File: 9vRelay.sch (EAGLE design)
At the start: 6 parts, among them K1 OJE-SS-109LMH, T1 2N3904

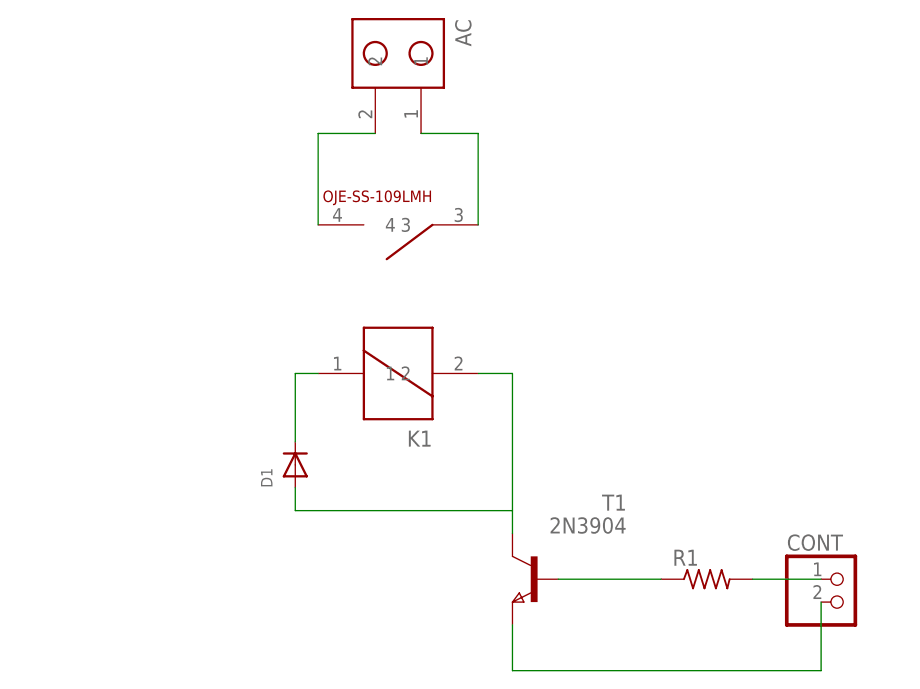
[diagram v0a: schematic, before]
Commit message: Re orientation and fixes
Re orientation and fixed the missing input voltage for powering the relay coil
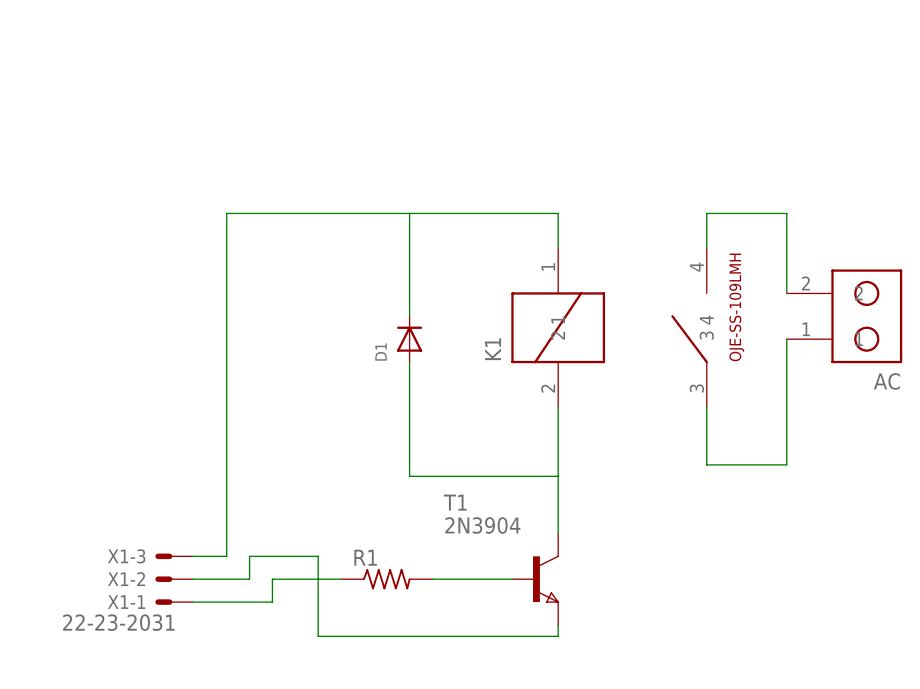
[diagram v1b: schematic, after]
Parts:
- removed CONT: (no value), pinhead:PINHD-1X2
- added X1: 22-23-2031, con-molex:22-23-2031
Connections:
- removed net N$4 (its old number): D1.C, K1.1
- removed net N$6: CONT.2, T1.E
- new net N$2: D1.C, K1.1, X1-3.S
- new net N$3: R1.1, X1-1.S
- net N$7: now also T1.E, X1-2.S; no longer CONT.1, R1.2
- net N$8: now also R1.2; no longer R1.1
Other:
- moved on the sheet: AC, D1, K1, R1
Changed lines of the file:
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@@
 <?xml version="1.0" encoding="utf-8"?>
 <!DOCTYPE eagle SYSTEM "eagle.dtd">
-<eagle version="7.3.0">
+<eagle version="7.4.0">
 <drawing>
 <settings>
@@
 <part name="K1" library="userdefined" deviceset="OJE-SS-109LMH" device=""/>
 <part name="T1" library="zetex" deviceset="FMMT451" device="" value="2N3904"/>
-<part name="CONT" library="pinhead" deviceset="PINHD-1X2" device=""/>
 <part name="AC" library="userdefined" deviceset="TBLOCK1X2" device=""/>
 <part name="R1" library="resistor" deviceset="R-US_" device="R0603"/>
 <part name="D1" library="adafruit" deviceset="DIODE" device="SMA"/>
+<part name="X1" library="con-molex" deviceset="22-23-2031" device=""/>
 </parts>
 <sheets>
@@
 </plain>
 <instances>
-<instance part="K1" gate="G$1" x="38.1" y="43.18" rot="R90"/>
-<instance part="T1" gate="G$1" x="53.34" y="10.16" rot="MR0"/>
-<instance part="CONT" gate="G$1" x="87.63" y="7.62"/>
-<instance part="AC" gate="G$1" x="38.1" y="68.58" rot="R270"/>
-<instance part="R1" gate="G$1" x="72.39" y="10.16"/>
-<instance part="D1" gate="G$1" x="26.67" y="22.86" rot="R90"/>
+<instance part="K1" gate="G$1" x="66.04" y="38.1"/>
+<instance part="T1" gate="G$1" x="53.34" y="10.16"/>
+<instance part="AC" gate="G$1" x="90.17" y="39.37" rot="R180"/>
+<instance part="R1" gate="G$1" x="36.83" y="10.16"/>
+<instance part="D1" gate="G$1" x="39.37" y="36.83" rot="R90"/>
+<instance part="X1" gate="-1" x="12.7" y="7.62" rot="R180"/>
+<instance part="X1" gate="-2" x="12.7" y="10.16" rot="R180"/>
+<instance part="X1" gate="-3" x="12.7" y="12.7" rot="R180"/>
 </instances>
 <busses>
 </busses>
 <nets>
+<net name="N$7" class="0">
+<segment>
+<pinref part="T1" gate="G$1" pin="E"/>
+<wire x1="29.21" y1="3.81" x2="55.88" y2="3.81" width="0.1524" layer="91"/>
+<wire x1="55.88" y1="3.81" x2="55.88" y2="5.08" width="0.1524" layer="91"/>
+<wire x1="29.21" y1="3.81" x2="29.21" y2="12.7" width="0.1524" layer="91"/>
+<wire x1="29.21" y1="12.7" x2="21.59" y2="12.7" width="0.1524" layer="91"/>
+<wire x1="21.59" y1="12.7" x2="21.59" y2="10.16" width="0.1524" layer="91"/>
+<pinref part="X1" gate="-2" pin="S"/>
+<wire x1="21.59" y1="10.16" x2="15.24" y2="10.16" width="0.1524" layer="91"/>
+</segment>
+</net>
+<net name="N$8" class="0">
+<segment>
+<pinref part="R1" gate="G$1" pin="2"/>
+<pinref part="T1" gate="G$1" pin="B"/>
+<wire x1="41.91" y1="10.16" x2="50.8" y2="10.16" width="0.1524" layer="91"/>
+</segment>
+</net>
 <net name="N$1" class="0">
 <segment>
+<pinref part="K1" gate="G$1" pin="2"/>
+<pinref part="T1" gate="G$1" pin="C"/>
+<wire x1="55.88" y1="29.21" x2="55.88" y2="21.59" width="0.1524" layer="91"/>
+<pinref part="D1" gate="G$1" pin="A"/>
+<wire x1="55.88" y1="21.59" x2="55.88" y2="15.24" width="0.1524" layer="91"/>
+<wire x1="39.37" y1="34.29" x2="39.37" y2="21.59" width="0.1524" layer="91"/>
+<wire x1="39.37" y1="21.59" x2="55.88" y2="21.59" width="0.1524" layer="91"/>
+</segment>
+</net>
+<net name="N$2" class="0">
+<segment>
+<pinref part="K1" gate="G$1" pin="1"/>
+<wire x1="55.88" y1="46.99" x2="55.88" y2="50.8" width="0.1524" layer="91"/>
+<pinref part="D1" gate="G$1" pin="C"/>
+<wire x1="55.88" y1="50.8" x2="39.37" y2="50.8" width="0.1524" layer="91"/>
+<wire x1="39.37" y1="50.8" x2="39.37" y2="39.37" width="0.1524" layer="91"/>
+<pinref part="X1" gate="-3" pin="S"/>
+<wire x1="15.24" y1="12.7" x2="19.05" y2="12.7" width="0.1524" layer="91"/>
+<wire x1="19.05" y1="12.7" x2="19.05" y2="50.8" width="0.1524" layer="91"/>
+<wire x1="19.05" y1="50.8" x2="39.37" y2="50.8" width="0.1524" layer="91"/>
+</segment>
+</net>
+<net name="N$4" class="0">
+<segment>
+<pinref part="K1" gate="G$1" pin="4"/>
+<wire x1="72.39" y1="46.99" x2="72.39" y2="50.8" width="0.1524" layer="91"/>
 <pinref part="AC" gate="G$1" pin="2"/>
-<pinref part="K1" gate="G$1" pin="4"/>
-<wire x1="35.56" y1="59.69" x2="29.21" y2="59.69" width="0.1524" layer="91"/>
-<wire x1="29.21" y1="59.69" x2="29.21" y2="49.53" width="0.1524" layer="91"/>
-</segment>
-</net>
-<net name="N$2" class="0">
-<segment>
+<wire x1="72.39" y1="50.8" x2="81.28" y2="50.8" width="0.1524" layer="91"/>
+<wire x1="81.28" y1="50.8" x2="81.28" y2="41.91" width="0.1524" layer="91"/>
+</segment>
+</net>
+<net name="N$11" class="0">
+<segment>
+<wire x1="81.28" y1="22.86" x2="72.39" y2="22.86" width="0.1524" layer="91"/>
+<pinref part="AC" gate="G$1" pin="1"/>
+<wire x1="81.28" y1="36.83" x2="81.28" y2="22.86" width="0.1524" layer="91"/>
 <pinref part="K1" gate="G$1" pin="3"/>
-<wire x1="46.99" y1="49.53" x2="46.99" y2="59.69" width="0.1524" layer="91"/>
-<pinref part="AC" gate="G$1" pin="1"/>
-<wire x1="46.99" y1="59.69" x2="40.64" y2="59.69" width="0.1524" layer="91"/>
+<wire x1="72.39" y1="29.21" x2="72.39" y2="22.86" width="0.1524" layer="91"/>
 </segment>
 </net>
 <net name="N$3" class="0">
 <segment>
-<pinref part="T1" gate="G$1" pin="C"/>
-<wire x1="50.8" y1="15.24" x2="50.8" y2="17.78" width="0.1524" layer="91"/>
-<pinref part="K1" gate="G$1" pin="2"/>
-<wire x1="50.8" y1="17.78" x2="50.8" y2="33.02" width="0.1524" layer="91"/>
-<wire x1="50.8" y1="33.02" x2="46.99" y2="33.02" width="0.1524" layer="91"/>
-<pinref part="D1" gate="G$1" pin="A"/>
-<wire x1="26.67" y1="20.32" x2="26.67" y2="17.78" width="0.1524" layer="91"/>
-<wire x1="26.67" y1="17.78" x2="50.8" y2="17.78" width="0.1524" layer="91"/>
-</segment>
-</net>
-<net name="N$4" class="0">
-<segment>
-<pinref part="D1" gate="G$1" pin="C"/>
-<wire x1="26.67" y1="25.4" x2="26.67" y2="33.02" width="0.1524" layer="91"/>
-<pinref part="K1" gate="G$1" pin="1"/>
-<wire x1="26.67" y1="33.02" x2="29.21" y2="33.02" width="0.1524" layer="91"/>
-</segment>
-</net>
-<net name="N$6" class="0">
-<segment>
-<pinref part="T1" gate="G$1" pin="E"/>
-<wire x1="50.8" y1="5.08" x2="50.8" y2="0" width="0.1524" layer="91"/>
-<pinref part="CONT" gate="G$1" pin="2"/>
-<wire x1="50.8" y1="0" x2="85.09" y2="0" width="0.1524" layer="91"/>
-<wire x1="85.09" y1="0" x2="85.09" y2="7.62" width="0.1524" layer="91"/>
-</segment>
-</net>
-<net name="N$7" class="0">
-<segment>
-<pinref part="CONT" gate="G$1" pin="1"/>
-<pinref part="R1" gate="G$1" pin="2"/>
-<wire x1="85.09" y1="10.16" x2="77.47" y2="10.16" width="0.1524" layer="91"/>
-</segment>
-</net>
-<net name="N$8" class="0">
-<segment>
+<pinref part="X1" gate="-1" pin="S"/>
+<wire x1="15.24" y1="7.62" x2="24.13" y2="7.62" width="0.1524" layer="91"/>
+<wire x1="24.13" y1="7.62" x2="24.13" y2="10.16" width="0.1524" layer="91"/>
 <pinref part="R1" gate="G$1" pin="1"/>
-<pinref part="T1" gate="G$1" pin="B"/>
-<wire x1="67.31" y1="10.16" x2="55.88" y2="10.16" width="0.1524" layer="91"/>
-</segment>
-</net>
+<wire x1="24.13" y1="10.16" x2="31.75" y2="10.16" width="0.1524" layer="91"/>
+</segment>
+</net>
